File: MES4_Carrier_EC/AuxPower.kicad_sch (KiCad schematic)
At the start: 37 parts, among them J14 IMU 9V, J15 SERVO 24V, J16 SCREEN 5V, J17 SERVO UART, SW2 SS12D10G5, U10 URB2405LD-20WR3, U9 URB2409S-10WR3

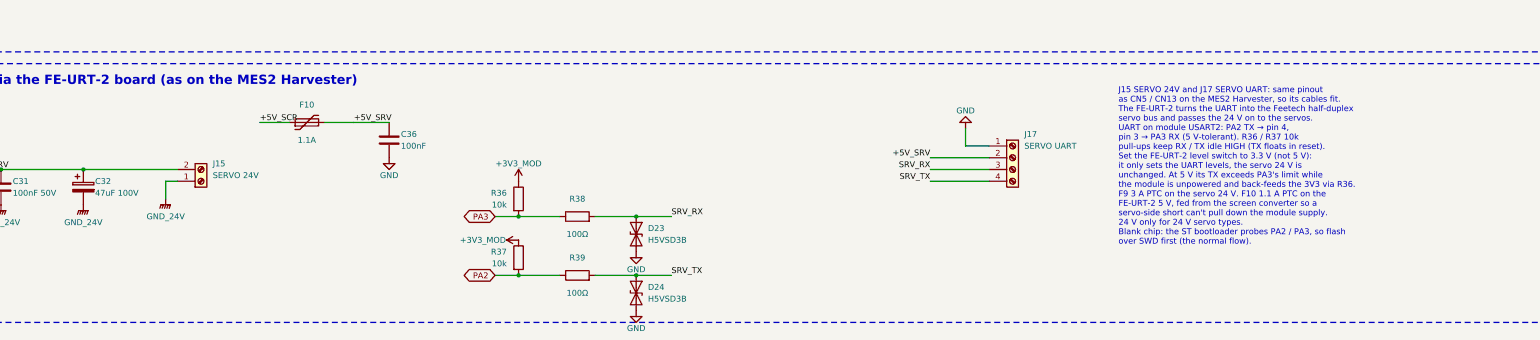
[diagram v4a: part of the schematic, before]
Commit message: Address design review R1: INA236, J15 polarity, review fixes
M1: U2-U5 are now TI INA236AIDDFR (C5443912, 50 V abs max, TSOT-23-8)
instead of the INA226 (40 V), since the SMBJ30A clamps at up to 48.4 V.
A project INA236 symbol keeps the INA226 body so the Flasher relay
wiring lands on the same pins; A1 and VBUS are gone (bus read on IN-),
addresses 0x40-0x43 via A0 = GND / VS / SDA / SCL. Same CONFIG / CAL /
MASK / ALERT values; notes give the 1.6 mV bus LSB and Device ID.
M3: J15 servo 24 V is pin 1 = +24 V like every power terminal.
L4: R38 servo RX series resistor 1k (limits PA3 back-feed).
L2: "current present" threshold 3 mA. L6: Power notes use 13 A / 2.2 W.
M2 / L5: silkscreen notes for "5V LOAD CELL - NEVER 24V" and
"CAN - NOT ETHERNET" (no keyed connector, by choice).
RJ45 1x4 footprint rebuilt from the HCTL drawing (14.0 mm ports,
Ø1.5 shield and Ø3.2 peg positions); U1 / U9 / U10 checked against the
JLC library and YLPTEC drawing. HANDOFF gains the review status table
and a layout checklist.

Co-Authored-By: Claude Opus 5.5 <noreply@anthropic.com>
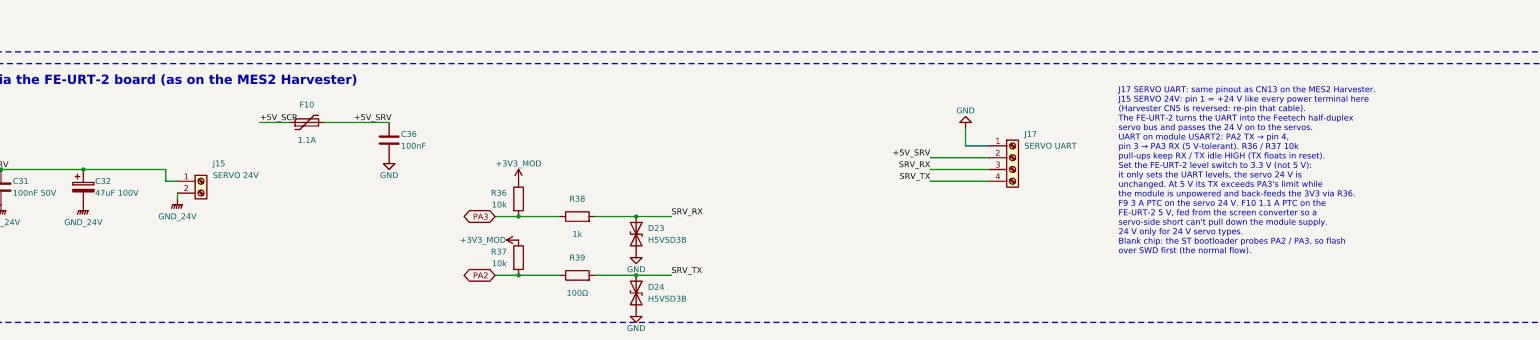
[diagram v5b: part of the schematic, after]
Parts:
- removed C36: 100nF, Capacitor_SMD:C_0402_1005Metric, symbol Device:C
- removed J15: SERVO 24V, MES4-Carrier-EC:CONN-TH_KF250NH-3.5-2P, symbol Connector:Screw_Terminal_01x02
- removed R36: 10k, Resistor_SMD:R_0402_1005Metric, symbol Device:R
- removed SW2: SS12D10G5, MES4-Carrier-EC:SW-TH_SHOU-HAN_SS12D10G4, symbol Switch:SW_SPDT
- removed TP9: +5V_SCR, TestPoint:TestPoint_THTPad_D2.0mm_Drill1.0mm, symbol Connector:TestPoint
- added C30: 47uF 100V, Capacitor_SMD:CP_Elec_8x10, symbol Device:C_Polarized
- added D22: SMF6.0A, Diode_SMD:D_SMF, symbol Device:D_Zener
- added D24: H5VSD3B, Diode_SMD:D_SOD-323, symbol Device:D_TVS
- added R37: 10k, Resistor_SMD:R_0402_1005Metric, symbol Device:R
- added R39: 100Ω, Resistor_SMD:R_0402_1005Metric, symbol Device:R
- C36: renamed from D23; value H5VSD3B -> 100nF; footprint Diode_SMD:D_SOD-323 -> Capacitor_SMD:C_0402_1005Metric; symbol Device:D_TVS -> Device:C; LCSC C20615806 -> C1525
- F10: renamed from R38; value 100Ω -> 1.1A; footprint Resistor_SMD:R_0402_1005Metric -> Fuse:Fuse_1206_3216Metric; symbol Device:R -> Device:Polyfuse; LCSC C25076 -> C126818
- J15: renamed from F10; value 1.1A -> SERVO 24V; footprint Fuse:Fuse_1206_3216Metric -> MES4-Carrier-EC:CONN-TH_KF250NH-3.5-2P; symbol Device:Polyfuse -> Connector:Screw_Terminal_01x02; LCSC C126818 -> C976556
- LED8: renamed from C30; value 47uF 100V -> Green; footprint Capacitor_SMD:CP_Elec_8x10 -> LED_SMD:LED_0805_2012Metric; symbol Device:C_Polarized -> Device:LED; LCSC C48935391 -> C2297
- R38: renamed from R39; value 100Ω -> 1k; LCSC C25076 -> C11702
- SW2: renamed from LED8; value Green -> SS12D10G5; footprint LED_SMD:LED_0805_2012Metric -> MES4-Carrier-EC:SW-TH_SHOU-HAN_SS12D10G4; symbol Device:LED -> Switch:SW_SPDT; LCSC C2297 -> C7431054
- TP9: renamed from D22; value SMF6.0A -> +5V_SCR; footprint Diode_SMD:D_SMF -> TestPoint:TestPoint_THTPad_D2.0mm_Drill1.0mm; symbol Device:D_Zener -> Connector:TestPoint; LCSC C19077499 -> (none)
- renumbered D24 to D23, R37 to R36
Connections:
- net +24V_AUX: now also C30.1; no longer LED8.1
- net +24V_SRV: now also J15.1 (Pin_1)
- net +3V3_MOD: now also R37.1
- net +5V_SCR: now also F10.1, TP9.1; no longer J15.1
- net +5V_SRV: now also C36.1, F10.2; no longer J15.2
- net +9V_IMU: now also SW2.2 (B)
- net GND: now also LED8.1 (K), D22.2 (A), D24.2 (A2); no longer SW2.1 (K), TP9.2 (A)
- net GND_24V: now also J15.2 (Pin_2), C30.2; no longer LED8.2
- net IMU_9V: now also SW2.1 (A)
- net PA2: now also R37.2, R39.1; no longer R36.2, R38.1
- net PA3: now also R36.2, R38.1; no longer F10.1
- net SRV_RX: now also D23.1 (A1), R38.2; no longer C36.1 (A1), F10.2
- net SRV_TX: now also D24.1 (A1), R39.2; no longer D23.1 (A1), R38.2
- net VBUS_SCR: now also D22.1 (K); no longer TP9.1 (K)
- net at R35.2: now also LED8.2 (A); no longer SW2.2 (A)
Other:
- note added: "J17 SERVO UART: same pinout as CN13 on the MES2 Harvester. J15 SERVO 24V: pin 1 = +24 V like every power terminal here (Harvester CN5 is reversed: re-pin that cable). The FE-URT-2 turns the UART into the Feetech half-duplex servo bus and passes the 24 V on to the servos. UART on module USART2: PA2 TX → pin 4, pin 3 → PA3 RX (5 V-tolerant). R36 / R37 10k pull-ups keep RX / TX idle HIGH (TX floats 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"
- note removed: "J15 SERVO 24V and J17 SERVO UART: same pinout as CN5 / CN13 on the MES2 Harvester, so its cables fit. The FE-URT-2 turns the UART into the Feetech half-duplex servo bus and passes the 24 V on to the servos. UART on module USART2: PA2 TX → pin 4, pin 3 → PA3 RX (5 V-tolerant). R36 / R37 10k pull-ups keep RX / TX idle HIGH (TX floats in reset). Set the FE-URT-2 level switch to 3.3 V (not 5 V): it o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"
- moved on the sheet: D23, LED8, R36, R38

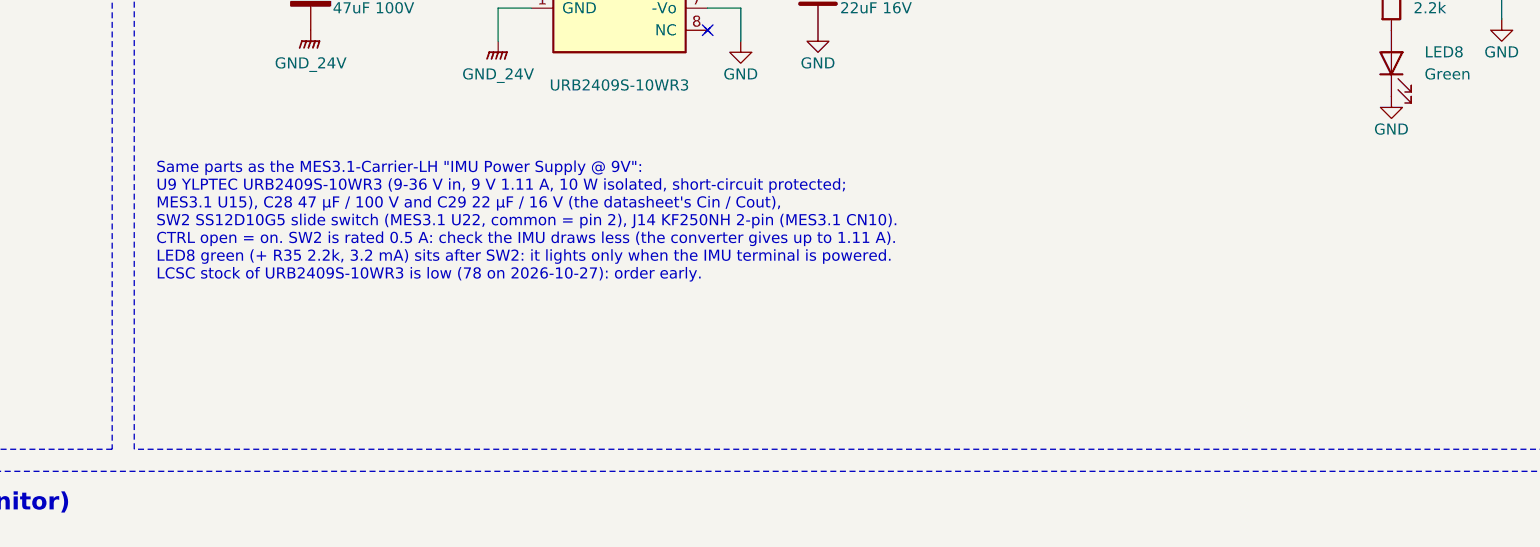
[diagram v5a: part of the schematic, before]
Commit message: Add whole-board LTspice simulations, IMU notes and the R2 review package
sim/: 16 LTspice benches grouped by schematic sheet (Power, Relays,
Sensors, LoadCell, AuxPower, IMU, Winch, Main) on the real supply chain
(DDR-480C-24 at 24 V and a 24 V Li-ion pack via XY-CD63L, diode-OR'd by
an Autoro AB20). run_sims.py runs them, make_report.py builds
report.html. All pass; the IEC 0.5 kV surge is not applicable to this
internal, isolated supply. Raw waveforms and logs are git-ignored.

IMU: 3DM-CV7-AHRS on the C-Series Connectivity Board (6212-3009). The
AuxPower and Main notes, README and HANDOFF now say J14's 9 V goes to the
board's Vaux only (never Vpri), not together with the USB cable; the
power budget uses the real ~0.02 A at 24 V.

review/: MES4-Carrier-EC_Review-Package_R2.pdf, 26 pages: changes since
R1, status of every R1 finding, open items, the simulation report and
the regenerated 11-page schematic. HANDOFF records the supply chain and
the M4 results.

Co-Authored-By: Claude Opus 5.5 <noreply@anthropic.com>
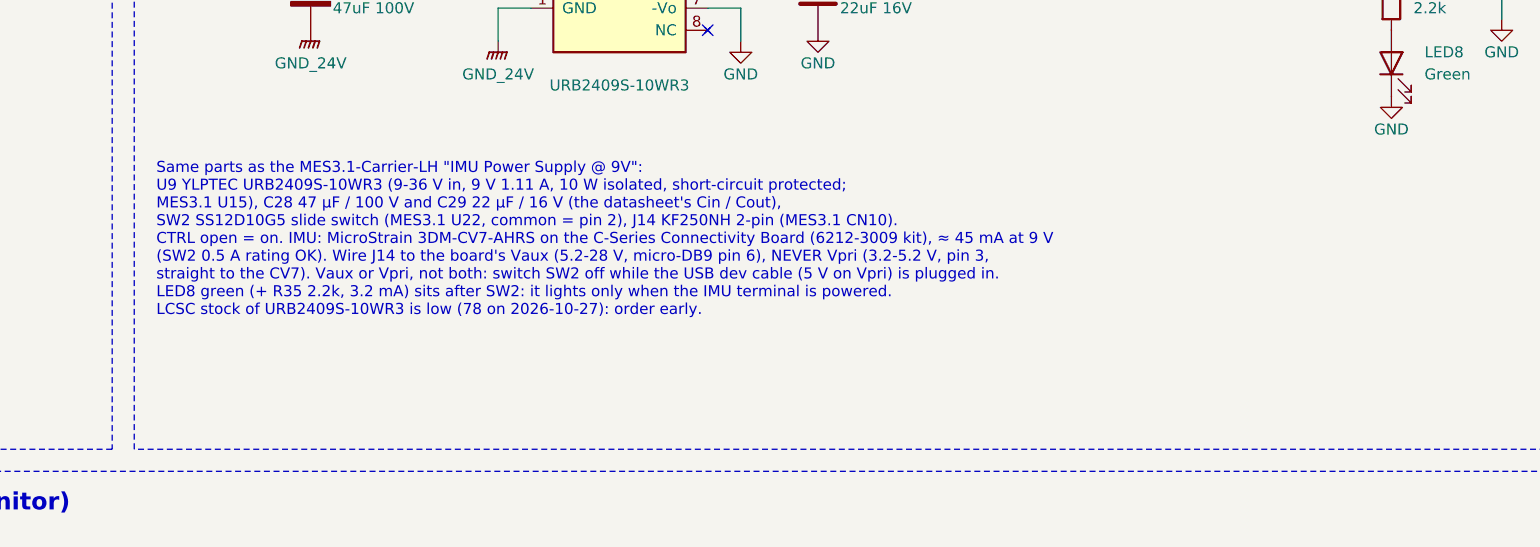
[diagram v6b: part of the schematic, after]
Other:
- note added: "Same parts as the MES3.1-Carrier-LH "IMU Power Supply @ 9V": U9 YLPTEC URB2409S-10WR3 (9-36 V in, 9 V 1.11 A, 10 W isolated, short-circuit protected; MES3.1 U15), C28 47 µF / 100 V and C29 22 µF / 16 V (the datasheet's Cin / Cout), SW2 SS12D10G5 slide switch (MES3.1 U22, common = pin 2), J14 KF250NH 2-pin (MES3.1 CN10). CTRL open = on. IMU: MicroStrain 3DM-CV7-AHRS on the C-Series Connectivity Bo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"
- note removed: "Same parts as the MES3.1-Carrier-LH "IMU Power Supply @ 9V": U9 YLPTEC URB2409S-10WR3 (9-36 V in, 9 V 1.11 A, 10 W isolated, short-circuit protected; MES3.1 U15), C28 47 µF / 100 V and C29 22 µF / 16 V (the datasheet's Cin / Cout), SW2 SS12D10G5 slide switch (MES3.1 U22, common = pin 2), J14 KF250NH 2-pin (MES3.1 CN10). CTRL open = on. SW2 is rated 0.5 A: check the IMU draws less (the converter g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"
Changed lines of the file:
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@@
 		(stroke (width 0) (type default))
 	)
-	(text "Same parts as the MES3.1-Carrier-LH \"IMU Power Supply @ 9V\":\nU9 YLPTEC URB2409S-10WR3 (9-36 V in, 9 V 1.11 A, 10 W isolated, short-circuit protected;\nMES3.1 U15), C28 47 µF / 100 V and C29 22 µF / 16 V (the datasheet's Cin / Cout),\nSW2 SS12D10G5 slide switch (MES3.1 U22, common = pin 2), J14 KF250NH 2-pin (MES3.1 CN10).\nCTRL open = on. SW2 is rated 0.5 A: check the IMU draws less (the converter gives up to 1.11 A).\nLED8 green (+ R35 2.2k, 3.2 mA) sits after SW2: it lights only when the IMU terminal is powered.\nLCSC stock of URB2409S-10WR3 is low (78 on 2026-10-27): order early."
+	(text "Same parts as the MES3.1-Carrier-LH \"IMU Power Supply @ 9V\":\nU9 YLPTEC URB2409S-10WR3 (9-36 V in, 9 V 1.11 A, 10 W isolated, short-circuit protected;\nMES3.1 U15), C28 47 µF / 100 V and C29 22 µF / 16 V (the datasheet's Cin / Cout),\nSW2 SS12D10G5 slide switch (MES3.1 U22, common = pin 2), J14 KF250NH 2-pin (MES3.1 CN10).\nCTRL open = on. IMU: MicroStrain 3DM-CV7-AHRS on the C-Series Connectivity Board (6212-3009 kit), ≈ 45 mA at 9 V\n(SW2 0.5 A rating OK). Wire J14 to the board's Vaux (5.2-28 V, micro-DB9 pin 6), NEVER Vpri (3.2-5.2 V, pin 3,\nstraight to the CV7). Vaux or Vpri, not both: switch SW2 off while the USB dev cable (5 V on Vpri) is plugged in.\nLED8 green (+ R35 2.2k, 3.2 mA) sits after SW2: it lights only when the IMU terminal is powered.\nLCSC stock of URB2409S-10WR3 is low (78 on 2026-10-27): order early."
 		(exclude_from_sim no)
 		(at 124.46 68.58 0)

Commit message: PCB placement, FE-URT-2 and GPS mounts, smaller screen converter, review R3
Placement: all terminals, USB-C and XT30 face the top edge (CAN DB9/RJ45 on
the sides), power block (U1, U9, U10, filters, GND joint) under the 24 V
input, relay bank and winch block below the terminal row, MES4-MCU slot
grouped with the Flasher's slot silkscreen. Feetech and GPS mounts parked
off-board until the layout is final.

Mounts: FE-URT-2 on 4 x YIYUAN SMTSOM320BTR M3 x 2 mm SMD standoffs (H6-H9,
C5301780) as on the MES3 carriers, board-only outline with a footprint
keep-out; simpleRTK4 Dual on 3 x SMTSOM365BTR M3 x 6.5 mm standoffs
(H10-H12, C5301796) + 12 mm spacers, with its STEP.

U10: URB2405LD-20WR3 (2" x 1") -> YLPTEC URB2405YMD-20WR3 (1" x 1",
C5369777), footprint from the JLC part checked against the Mornsun drawing;
C38 100 uF / 16 V output bulk (C81993) per its datasheet. AUX1 re-run:
3.58 A start-up peak vs 4.4 A OCP, 3.0 A at 4.94 V. Review package R3.

Generator: new parts take UUIDs from their own counter range so no PCB link
moves; import_footprints.py --add-missing; group_footprints.py never moves
placed parts and stops once groups are edited in KiCad.

Co-Authored-By: Claude Opus 5.5 <noreply@anthropic.com>
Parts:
- added C38: 100uF 16V, Capacitor_SMD:CP_Elec_6.3x5.4, symbol Device:C_Polarized
- added H10, H11, H12: M3 standoff 6.5mm, MES4-Carrier-EC:Standoff_SMD_M3_H6.5mm_SMTSOM365BTR, symbol Mechanical:MountingHole
- added H6, H7, H8, H9: M3 standoff 2mm, MES4-Carrier-EC:Standoff_SMD_M3_H2mm_SMTSOM320BTR, symbol Mechanical:MountingHole
- U10: value URB2405LD-20WR3 -> URB2405YMD-20WR3; footprint MES4-Carrier-EC:PWRM-TH_YLPTEC_URBXXXXLD-20WR3 -> MES4-Carrier-EC:PWRM-TH_YLPTEC_URBXXXXYMD-20WR3; symbol MES4-Carrier-EC:URB2405LD-20WR3 -> MES4-Carrier-EC:URB2405YMD-20WR3; LCSC C5369825 -> C5369777
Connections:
- net +24V_AUX: now also U10.3 (+Vin); no longer U10.2 (+Vin)
- net +5V_SCR: now also U10.4 (+Vo), C38.1; no longer U10.3 (+Vo)
- net GND: now also U10.6 (GND), C38.2; no longer U10.5 (GND)
- net GND_24V: now also U10.2 (-Vin); no longer U10.1 (-Vin)
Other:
- note added: "FE-URT-2 mount: H6-H9 M3 x 2 mm SMD standoffs (SMTSOM320BTR) on its 48.5 x 28.7 mm holes, M3 screws from the top. No parts under it. GPS (ArduSimple simpleRTK4 Dual) stacked above it: H10-H12 M3 x 6.5 mm SMD standoffs (SMTSOM365BTR) + M3 x 12 mm male-female spacers (fitted by hand) on its left-bottom, left-top and right holes; underside 18.5 mm up. The RTK is powered from its own GPS USB-C. Stand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"
- note added: "U10 YLPTEC URB2405YMD-20WR3: 9-36 V in (40 V max, 50 V 1 s surge), 5 V 4 A, 20 W isolated, short-circuit protected, 1" x 1" DIP. CTRL and Trim open (on, 5.0 V). C30 47 µF + C27 100 µF on +24V_AUX (datasheet Cin 100 µF / 50 V); C38 100 µF / 16 V bulk (Cout 100 µF / 16 V) + C33 / C34 22 µF + C35 100 nF. F11 3 A PTC (same part as the relay outputs) + D22 SMF6.0A, then J16: the MES4-Flasher's USB-C p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"
- note removed: "U10 YLPTEC URB2405LD-20WR3: 9-36 V in, 5 V 4 A, 20 W isolated, short-circuit protected, 2" x 1" DIP. CTRL and Trim open (on, 5.0 V). C30 47 µF (datasheet C1 47-100 µF), C33 / C34 22 µF (C2 / C3 10-22 µF). F11 3 A PTC (same part as the relay outputs) + D22 SMF6.0A, then J16: the MES4-Flasher's USB-C power-only receptacle, rated 5 V 3 A (3 A on VBUS; GND pins 1.25 A each). R41 / R40 10k Rp to 5 V o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"
